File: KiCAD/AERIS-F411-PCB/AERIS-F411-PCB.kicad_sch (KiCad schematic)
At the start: 0 parts

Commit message: solve issue of power sheet
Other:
- sheet POWER SECTION ports: added U10_VCC; removed none
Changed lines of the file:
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@@
+			)
+		)
+		(pin "U10_VCC" output
+			(at 76.2 58.42 0)
+			(effects
+				(font
+					(size 1.27 1.27)
+				)
+				(justify right)
 			)
 		)

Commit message: Update_in_Power_Section
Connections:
- no-connect marks 0 -> 9
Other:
- sheet POWER SECTION ports: added +3.3V_SENSOR, USB_FS_DM, USB_FS_DP; removed USB_DM, USB_DP
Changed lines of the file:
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@@
 		(rev "1")
+	)
+	(no_connect
+		(at 76.2 64.77)
+	)
+	(no_connect
+		(at 62.23 25.4)
+	)
+	(no_connect
+		(at 25.4 34.29)
+	)
+	(no_connect
+		(at 76.2 58.42)
+	)
+	(no_connect
+		(at 55.88 25.4)
+	)
+	(no_connect
+		(at 76.2 43.18)
+	)
+	(no_connect
+		(at 25.4 43.18)
+	)
+	(no_connect
+		(at 76.2 34.29)
+	)
+	(no_connect
+		(at 53.34 73.66)
 	)
 	(sheet
@@
 			)
 		)
-		(pin "USB_DM" bidirectional
-			(at 25.4 55.88 180)
-			(effects
-				(font
-					(size 1.27 1.27)
-				)
-				(justify left)
-			)
-		)
-		(pin "USB_DP" bidirectional
-			(at 25.4 63.5 180)
-			(effects
-				(font
-					(size 1.27 1.27)
-				)
-				(justify left)
-			)
-		)
 		(pin "VIN" output
 			(at 76.2 64.77 0)
@@
 			(effects
 				(font
+					(size 1.27 1.27)
+				)
+				(justify right)
+			)
+		)
+		(pin "+3.3V_SENSOR" output
+			(at 53.34 73.66 270)
+			(effects
+				(font
+					(size 1.27 1.27)
+				)
+				(justify left)
+			)
+		)
+		(pin "USB_FS_DM" bidirectional
+			(at 62.23 25.4 90)
+			(effects
+				(font
+					(size 1.27 1.27)
+				)
+				(justify right)
+			)
+		)
+		(pin "USB_FS_DP" bidirectional
+			(at 55.88 25.4 90)
+			(effects
+				(font

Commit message: updated
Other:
- added sheet MCU_Core (MCU_Core.kicad_sch)
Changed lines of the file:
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@@
 	)
 	(no_connect
-		(at 62.23 25.4)
+		(at 25.4 63.5)
 	)
 	(no_connect
@@
 	)
 	(no_connect
-		(at 55.88 25.4)
+		(at 25.4 53.34)
 	)
 	(no_connect
@@
 		)
 		(pin "USB_FS_DM" bidirectional
-			(at 62.23 25.4 90)
+			(at 25.4 63.5 180)
 			(effects
 				(font
 					(size 1.27 1.27)
 				)
-				(justify right)
+				(justify left)
 			)
 		)
 		(pin "USB_FS_DP" bidirectional
-			(at 55.88 25.4 90)
+			(at 25.4 53.34 180)
 			(effects
 				(font
 					(size 1.27 1.27)
 				)
-				(justify right)
+				(justify left)
 			)
 		)
@@
 				)
 			)
+		)
+	)
+	(sheet
+		(at 110.49 71.12)
+		(size 63.5 120.65)
+		(exclude_from_sim no)
+		(in_bom yes)
+		(on_board yes)
+		(dnp no)
+		(fields_autoplaced yes)
+		(stroke
+			(width 0.1524)
+			(type solid)
+		)
+		(fill
+			(color 0 0 0 0)
+		)
+		(property "Sheetname" "MCU_Core"
+			(at 110.49 70.4084 0)
+			(show_name yes)
+			(do_not_autoplace no)
+			(effects
+				(font
+					(size 1.27 1.27)
+				)
+				(justify left bottom)
+			)
+		)
+		(property "Sheetfile" "MCU_Core.kicad_sch"
+			(at 110.49 192.3546 0)
+			(show_name yes)
+			(do_not_autoplace no)
+			(effects
+				(font
+					(size 1.27 1.27)
+				)
+				(justify left top)
+			)
+		)
+		(instances
+			(project "AERIS-F411-PCB"
+				(path "/41f25c5f-e761-4f33-a9f5-6d8db67ffdd9"
+					(page "3")
+				)
+			)

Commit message: MCU Core ADDED
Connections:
- no-connect marks 9 -> 10
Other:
- sheet MCU_Core ports: added 3.3V; removed none
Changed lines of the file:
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@@
+	)
+	(no_connect
+		(at 173.99 147.32)
 	)
 	(no_connect
@@
 			)
 		)
+		(pin "3.3V" input
+			(at 173.99 147.32 0)
+			(effects
+				(font
+					(size 1.27 1.27)
+				)
+				(justify right)
+			)
+		)

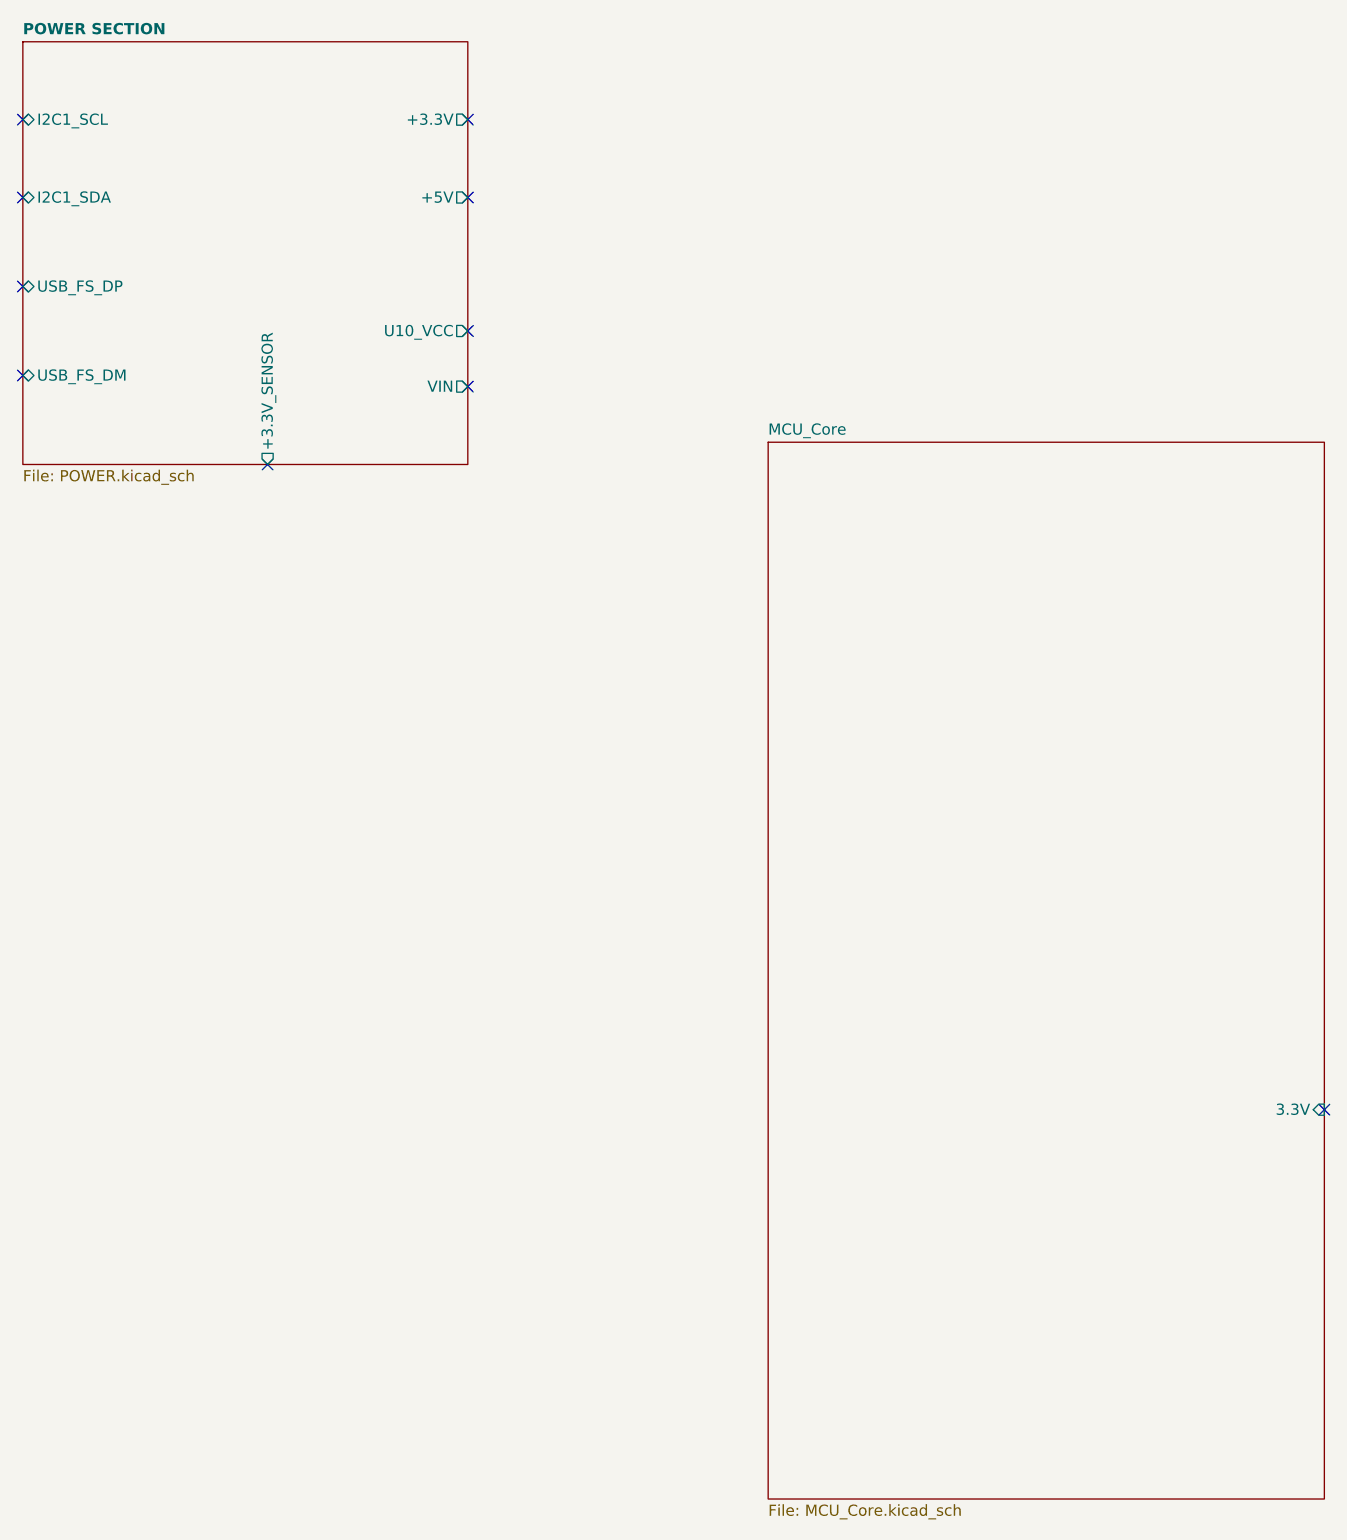
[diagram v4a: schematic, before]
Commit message: Added Memory/Storage sheet
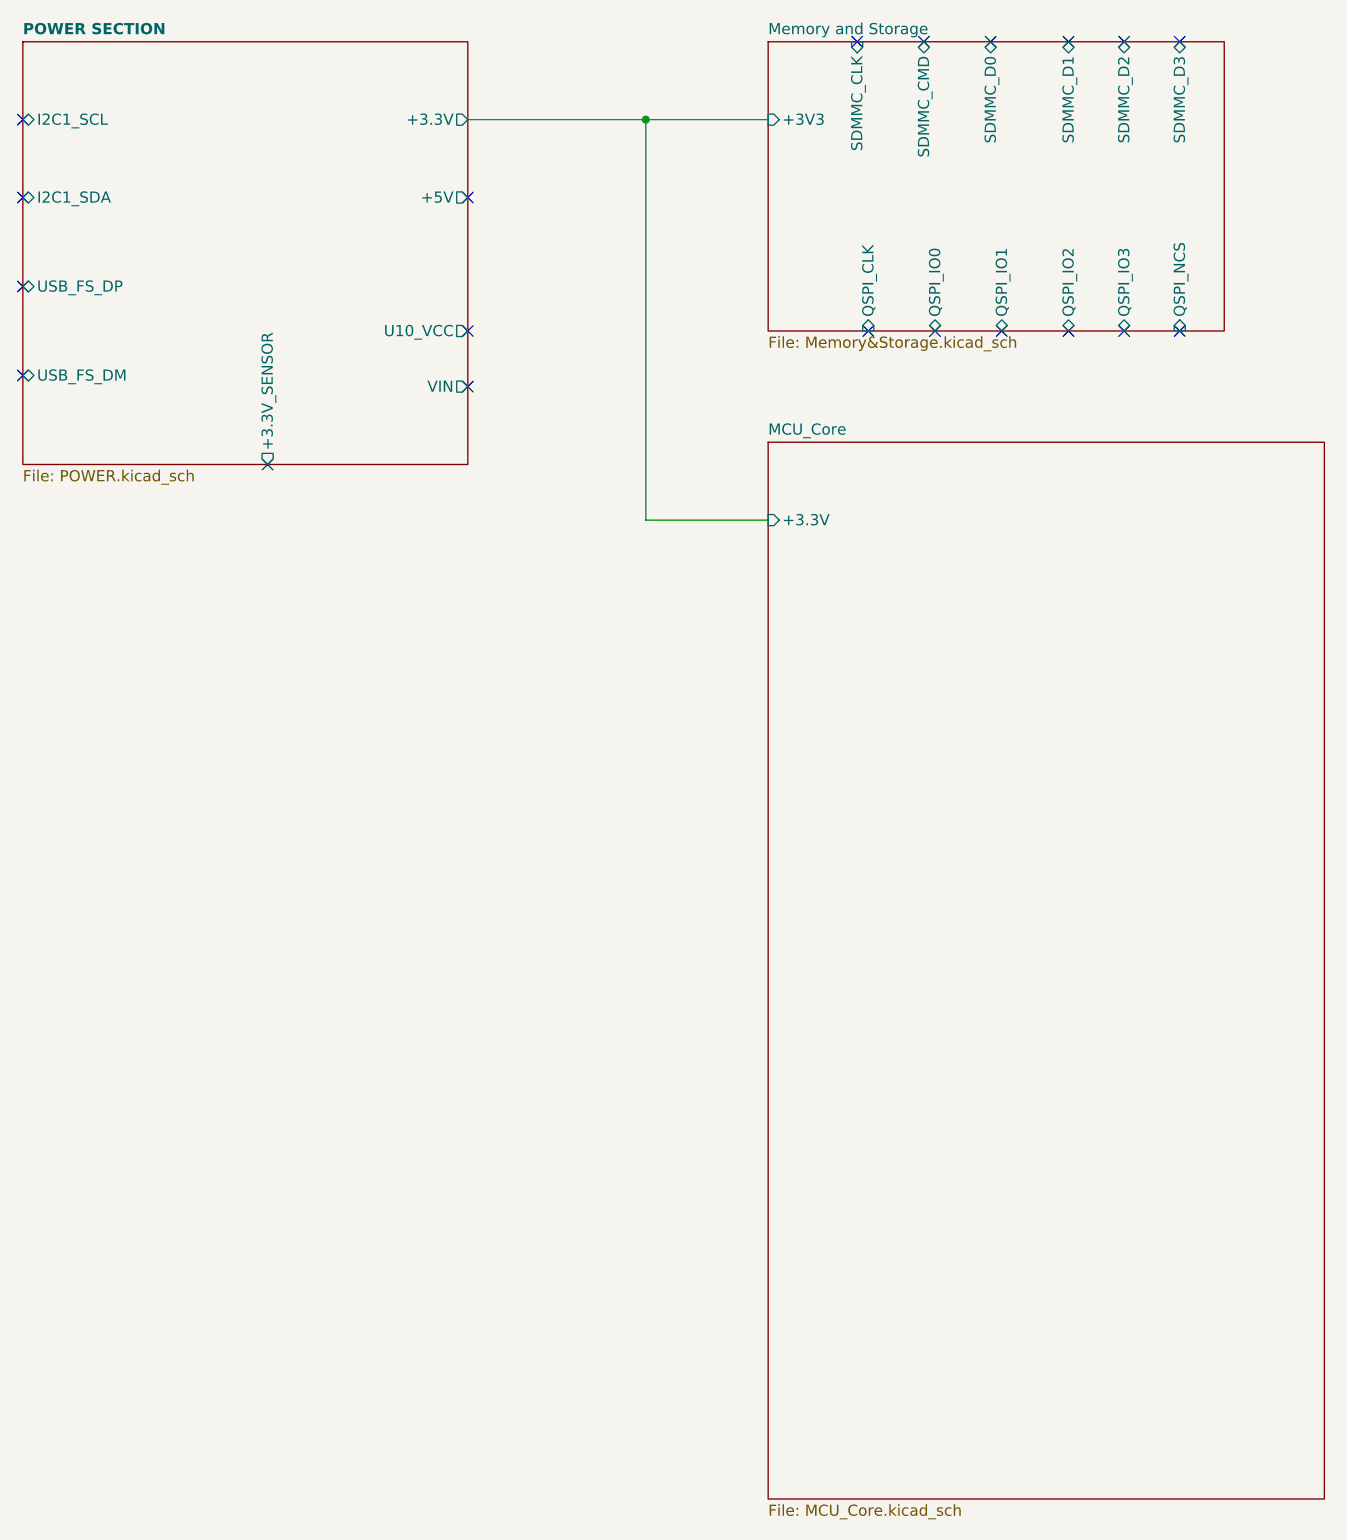
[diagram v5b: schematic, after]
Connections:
- no-connect marks 10 -> 20
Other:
- added sheet Memory and Storage (Memory&Storage.kicad_sch)
- sheet MCU_Core ports: added +3.3V; removed 3.3V

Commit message: update
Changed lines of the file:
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@@
 	(wire
 		(pts
-			(xy 96.52 34.29) (xy 96.52 80.01)
-		)
-		(stroke
-			(width 0)
-			(type default)
-		)
-	)
-	(wire
-		(pts
-			(xy 96.52 80.01) (xy 110.49 80.01)
+			(xy 96.52 34.29) (xy 96.52 74.93)
+		)
+		(stroke
+			(width 0)
+			(type default)
+		)
+	)
+	(wire
+		(pts
+			(xy 96.52 74.93) (xy 110.49 74.93)
 		)
 		(stroke
@@
 		)
 		(pin "+3.3V" input
-			(at 110.49 80.01 180)
-			(effects
-				(font
+			(at 110.49 74.93 180)
+			(effects
+				(font
